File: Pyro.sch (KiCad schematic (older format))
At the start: 14 parts

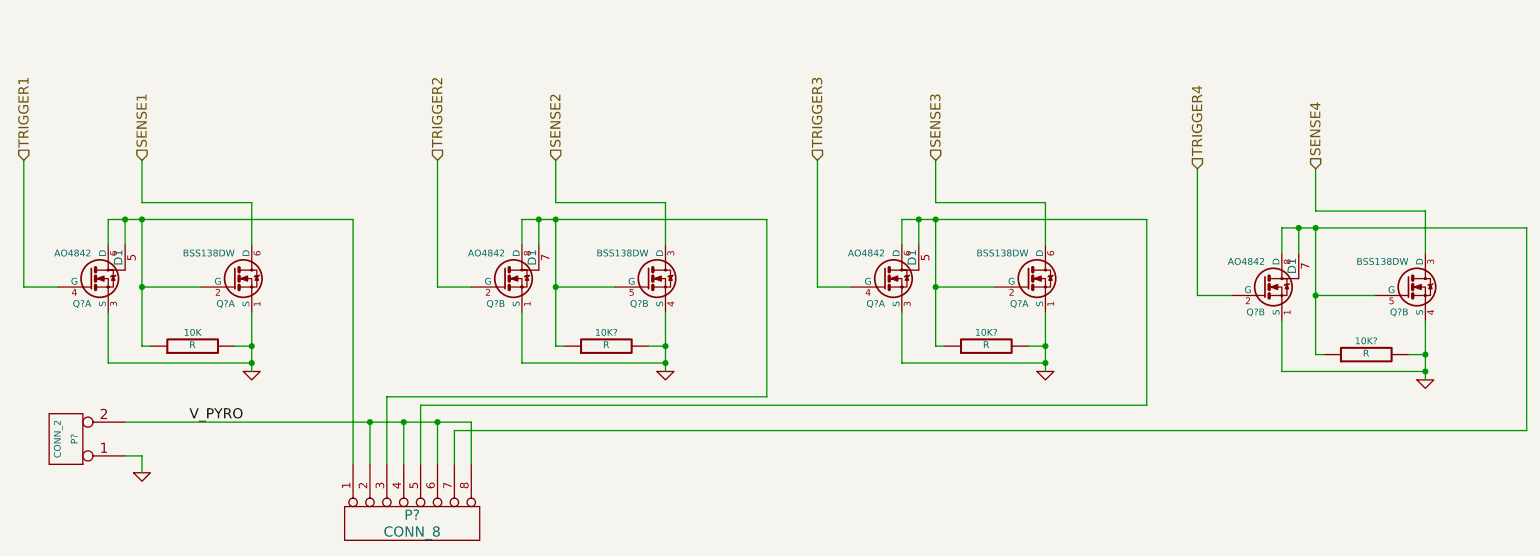
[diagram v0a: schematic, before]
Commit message: Added pyro circuits
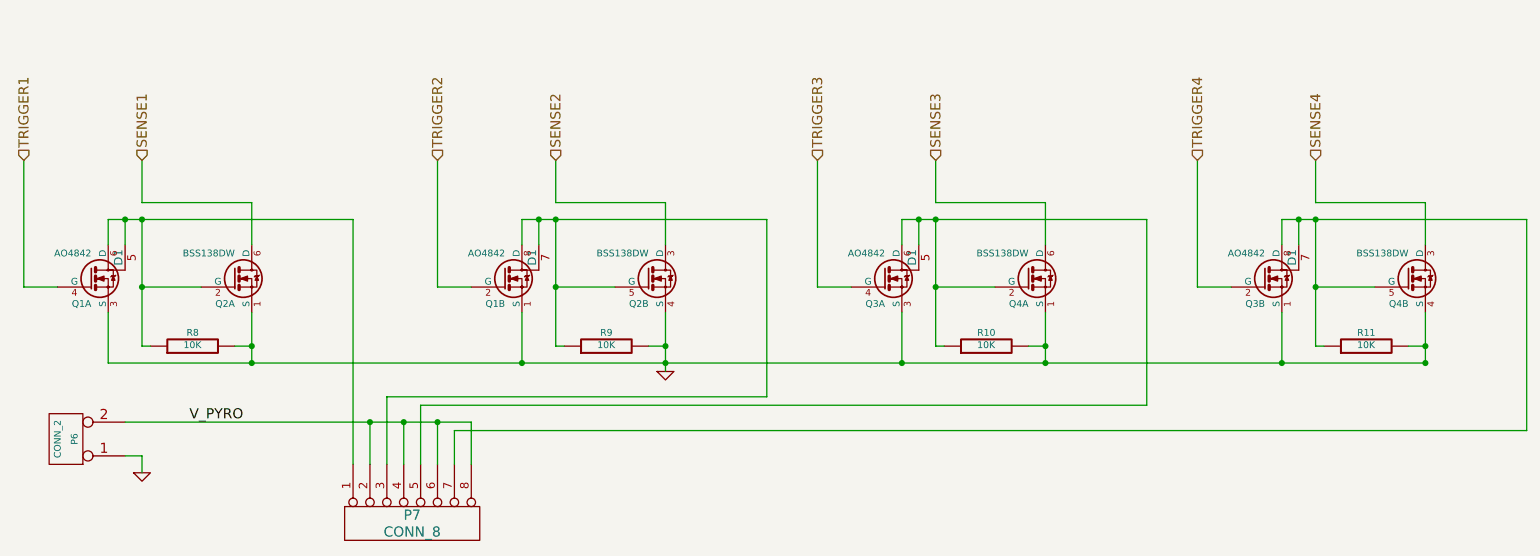
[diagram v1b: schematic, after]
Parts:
- P6: renamed from P?; footprint (none) -> Pin_Headers:Pin_Header_Straight_1x02
- P7: renamed from P?; footprint (none) -> Pin_Headers:Pin_Header_Straight_1x08
- Q1, Q3: renamed from Q?; footprint (none) -> Housings_SOIC:SOIC-8_3.9x4.9mm_Pitch1.27mm
- Q2, Q4: renamed from Q?; footprint (none) -> Housings_SOT-23_SOT-143_TSOT-6:SC70-6_Handsoldering
- R10, R11, R9: renamed from 10K?; value R -> 10K; footprint ~ -> Resistors_SMD:R_0805_HandSoldering
- R8: renamed from 10K; value R -> 10K; footprint ~ -> Resistors_SMD:R_0805_HandSoldering
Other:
- moved on the sheet: Q3B, Q4B, R11

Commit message: New MOSFETs
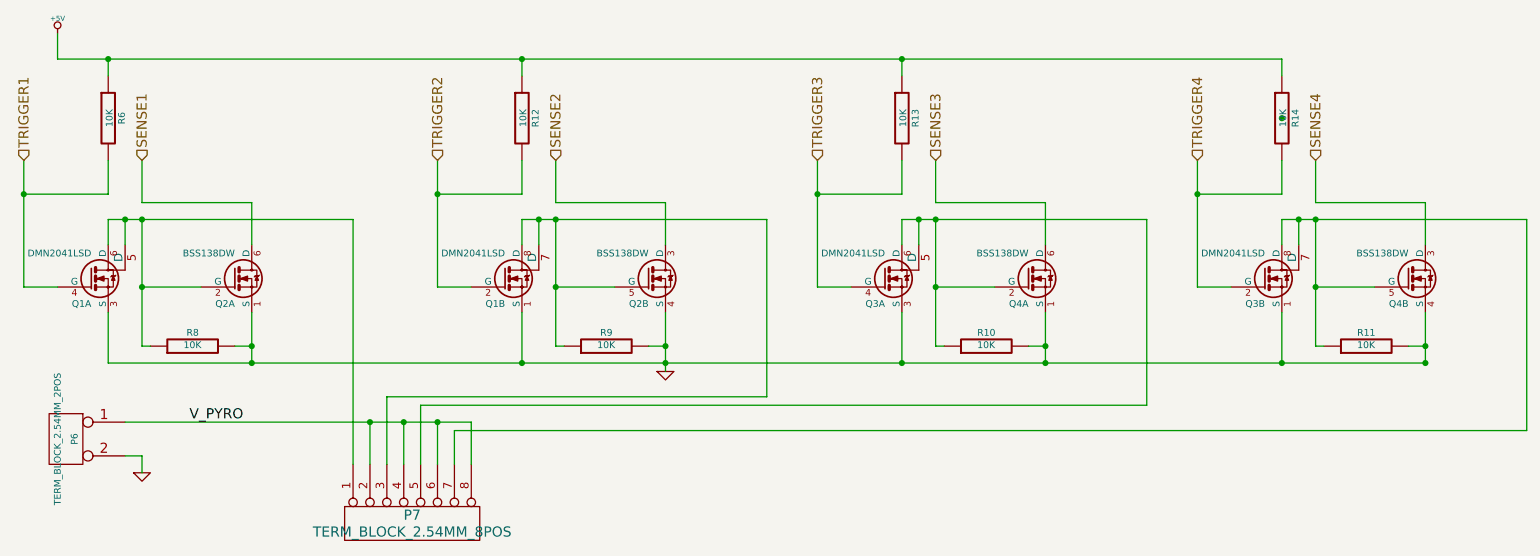
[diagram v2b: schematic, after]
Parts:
- removed P6: CONN_2, Pin_Headers:Pin_Header_Straight_1x02, symbol CONN_2
- removed P7: CONN_8, Pin_Headers:Pin_Header_Straight_1x08, symbol CONN_8
- removed Q1, Q3: AO4842, Housings_SOIC:SOIC-8_3.9x4.9mm_Pitch1.27mm, symbol AO4842
- added P6: TERM_BLOCK_2.54MM_2POS, symbol TERM_BLOCK_2.54MM_2POS
- added P7: TERM_BLOCK_2.54MM_8POS, symbol TERM_BLOCK_2.54MM_8POS
- added Q1, Q3: DMN2041LSD, symbol DMN2041LSD
- added R12, R13, R14, R6: 10K, ~, symbol R
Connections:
- net GND: now also P6.2 (PM), Q1.1 (S), Q1.3 (S), Q3.1 (S), Q3.3 (S)
- net TRIGGER1: now also Q1.4 (G), R6.2
- net TRIGGER2: now also Q1.2 (G), R12.2
- net TRIGGER3: now also Q3.4 (G), R13.2
- net TRIGGER4: now also Q3.2 (G), R14.2
- net V_PYRO: now also P6.1 (P1), P7.2 (P2), P7.4 (P4), P7.6 (P6), P7.8 (P8)
- net at Q2.2 (G), R8.1: now also P7.1 (P1), Q1.5 (D), Q1.6 (D)
- net at Q2.5 (G), R9.1: now also P7.3 (P3), Q1.7 (D), Q1.8 (D)
- net at Q4.2 (G), R10.1: now also P7.5 (P5), Q3.5 (D), Q3.6 (D)
- net at Q4.5 (G), R11.1: now also P7.7 (P7), Q3.7 (D), Q3.8 (D)
- new net +5V: R12.1, R13.1, R14.1, R6.1
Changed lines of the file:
@@
 LIBS:xbee
 LIBS:avbay-cache
-EELAYER 25 0
+EELAYER 27 0
 EELAYER END
 $Descr A4 11693 8268
@@
 Sheet 4 4
 Title ""
-Date "4 dec 2014"
+Date "6 dec 2014"
 Rev ""
 Comp ""
@@
 TRIGGER1
 $Comp
-L CONN_2 P6
-U 1 1 548101EA
-P 950 3400
-F 0 "P6" V 900 3400 40  0000 C CNN
-F 1 "CONN_2" V 1000 3400 40  0000 C CNN
-F 2 "Pin_Headers:Pin_Header_Straight_1x02" H 950 3400 60  0001 C CNN
-F 3 "" H 950 3400 60  0000 C CNN
-	1    950  3400
-	-1   0    0    1
-$EndComp
-$Comp
-L GND #PWR030
+L GND #PWR31
 U 1 1 54810205
 P 1400 3600
-F 0 "#PWR030" H 1400 3600 30  0001 C CNN
+F 0 "#PWR31" H 1400 3600 30  0001 C CNN
 F 1 "GND" H 1400 3530 30  0001 C CNN
 F 2 "" H 1400 3600 60  0000 C CNN
@@
 	1    1400 3600
 	1    0    0    -1
-$EndComp
-$Comp
-L CONN_8 P7
-U 1 1 54810218
-P 3000 3900
-F 0 "P7" V 2950 3900 60  0000 C CNN
-F 1 "CONN_8" V 3050 3900 60  0000 C CNN
-F 2 "Pin_Headers:Pin_Header_Straight_1x08" H 3000 3900 60  0001 C CNN
-F 3 "" H 3000 3900 60  0000 C CNN
-	1    3000 3900
-	0    -1   1    0
 $EndComp
 $Comp
@@
 $EndComp
 $Comp
-L AO4842 Q1
-U 1 1 54810736
-P 1100 2450
-F 0 "Q1" H 1100 2301 40  0000 R CNN
-F 1 "AO4842" H 1100 2600 40  0000 R CNN
-F 2 "Housings_SOIC:SOIC-8_3.9x4.9mm_Pitch1.27mm" H 970 2552 29  0001 C CNN
-F 3 "~" H 1100 2450 60  0000 C CNN
-	1    1100 2450
-	1    0    0    -1
-$EndComp
-$Comp
 L BSS138DW Q2
 U 1 1 54810890
@@
 TRIGGER2
 $Comp
-L GND #PWR031
+L GND #PWR32
 U 1 1 54810E85
 P 4500 3000
-F 0 "#PWR031" H 4500 3000 30  0001 C CNN
+F 0 "#PWR32" H 4500 3000 30  0001 C CNN
 F 1 "GND" H 4500 2930 30  0001 C CNN
 F 2 "" H 4500 3000 60  0000 C CNN
@@
 $EndComp
 $Comp
-L AO4842 Q3
-U 1 1 54810F68
-P 5800 2450
-F 0 "Q3" H 5800 2301 40  0000 R CNN
-F 1 "AO4842" H 5800 2600 40  0000 R CNN
-F 2 "Housings_SOIC:SOIC-8_3.9x4.9mm_Pitch1.27mm" H 5670 2552 29  0001 C CNN
-F 3 "~" H 5800 2450 60  0000 C CNN
-	1    5800 2450
-	1    0    0    -1
-$EndComp
-$Comp
 L BSS138DW Q4
 U 1 1 54810F77
@@
 $EndComp
 $Comp
-L AO4842 Q3
-U 2 1 54810FE4
-P 8050 2450
-F 0 "Q3" H 8050 2301 40  0000 R CNN
-F 1 "AO4842" H 8050 2600 40  0000 R CNN
-F 2 "Housings_SOIC:SOIC-8_3.9x4.9mm_Pitch1.27mm" H 7920 2552 29  0001 C CNN
-F 3 "~" H 8050 2450 60  0000 C CNN
-	2    8050 2450
-	1    0    0    -1
-$EndComp
-$Comp
 L BSS138DW Q4
 U 2 1 54810FF3
@@
 	1    0    0    -1
 $EndComp
-$Comp
-L AO4842 Q1
-U 2 1 548110D2
-P 3550 2450
-F 0 "Q1" H 3550 2301 40  0000 R CNN
-F 1 "AO4842" H 3550 2600 40  0000 R CNN
-F 2 "Housings_SOIC:SOIC-8_3.9x4.9mm_Pitch1.27mm" H 3420 2552 29  0001 C CNN
-F 3 "~" H 3550 2450 60  0000 C CNN
-	2    3550 2450
-	1    0    0    -1
-$EndComp
 Text Label 2000 3300 2    60   ~ 0
 V_PYRO
@@
 Wire Wire Line
 	9000 2950 9000 2650
+Wire Wire Line
+	900  1000 900  1150
+Wire Wire Line
+	900  1150 8150 1150
+$Comp
+L R R6
+U 1 1 548277E3
+P 1200 1500
+F 0 "R6" V 1280 1500 40  0000 C CNN
+F 1 "10K" V 1207 1501 40  0000 C CNN
+F 2 "~" V 1130 1500 30  0000 C CNN
+F 3 "~" H 1200 1500 30  0000 C CNN
+	1    1200 1500
+	1    0    0    -1
+$EndComp
+Wire Wire Line
+	1200 1750 1200 1950
+Wire Wire Line
+	1200 1950 700  1950
+Connection ~ 700  1950
+Wire Wire Line
+	1200 1250 1200 1150
+Connection ~ 1200 1150
+$Comp
+L R R12
+U 1 1 548278C1
+P 3650 1500
+F 0 "R12" V 3730 1500 40  0000 C CNN
+F 1 "10K" V 3657 1501 40  0000 C CNN
+F 2 "~" V 3580 1500 30  0000 C CNN
+F 3 "~" H 3650 1500 30  0000 C CNN
+	1    3650 1500
+	1    0    0    -1
+$EndComp
+$Comp
+L R R14
+U 1 1 548278CC
+P 8150 1500
+F 0 "R14" V 8230 1500 40  0000 C CNN
+F 1 "10K" V 8157 1501 40  0000 C CNN
+F 2 "~" V 8080 1500 30  0000 C CNN
+F 3 "~" H 8150 1500 30  0000 C CNN
+	1    8150 1500
+	1    0    0    -1
+$EndComp
+$Comp
+L R R13
+U 1 1 548278D2
+P 5900 1500
+F 0 "R13" V 5980 1500 40  0000 C CNN
+F 1 "10K" V 5907 1501 40  0000 C CNN
+F 2 "~" V 5830 1500 30  0000 C CNN
+F 3 "~" H 5900 1500 30  0000 C CNN
+	1    5900 1500
+	1    0    0    -1
+$EndComp
+Wire Wire Line
+	8150 1150 8150 1250
+Wire Wire Line
+	8150 1750 8150 1950
+Wire Wire Line
+	8150 1950 7650 1950
+Connection ~ 7650 1950
+Wire Wire Line
+	5900 1150 5900 1250
+Connection ~ 5900 1150
+Wire Wire Line
+	5900 1750 5900 1950
+Wire Wire Line
+	5900 1950 5400 1950
+Connection ~ 5400 1950
+Wire Wire Line
+	3650 1750 3650 1950
+Wire Wire Line
+	3650 1950 3150 1950
+Connection ~ 3150 1950
+Wire Wire Line
+	3650 1250 3650 1150
+Connection ~ 3650 1150
+$Comp
+L +5V #PWR30
+U 1 1 5482887D
+P 900 1000
+F 0 "#PWR30" H 900 1090 20  0001 C CNN
+F 1 "+5V" H 900 1090 30  0000 C CNN
+F 2 "" H 900 1000 60  0000 C CNN
+F 3 "" H 900 1000 60  0000 C CNN
+	1    900  1000
+	1    0    0    -1
+$EndComp
+$Comp
+L TERM_BLOCK_2.54MM_2POS P6
+U 1 1 5482AD9E
+P 950 3400
+F 0 "P6" V 900 3400 40  0000 C CNN
+F 1 "TERM_BLOCK_2.54MM_2POS" V 1000 3400 40  0000 C CNN
+F 2 "" H 950 3400 60  0000 C CNN
+F 3 "" H 950 3400 60  0000 C CNN
+	1    950  3400
+	-1   0    0    -1
+$EndComp
+$Comp
+L TERM_BLOCK_2.54MM_8POS P7
+U 1 1 5482ADAD
+P 3000 3900
+F 0 "P7" V 2950 3900 60  0000 C CNN
+F 1 "TERM_BLOCK_2.54MM_8POS" V 3050 3900 60  0000 C CNN
+F 2 "" H 3000 3900 60  0000 C CNN
+F 3 "" H 3000 3900 60  0000 C CNN
+	1    3000 3900
+	0    -1   1    0
+$EndComp
+Connection ~ 8150 1500
+$Comp
+L DMN2041LSD Q1
+U 1 1 5482D60C
+P 1100 2450
+F 0 "Q1" H 1100 2301 40  0000 R CNN
+F 1 "DMN2041LSD" H 1100 2600 40  0000 R CNN
+F 2 "" H 970 2552 29  0000 C CNN
+F 3 "" H 1100 2450 60  0000 C CNN
+	1    1100 2450
+	1    0    0    -1
+$EndComp
+$Comp
+L DMN2041LSD Q3
+U 1 1 5482D619
+P 5800 2450
+F 0 "Q3" H 5800 2301 40  0000 R CNN
+F 1 "DMN2041LSD" H 5800 2600 40  0000 R CNN
+F 2 "" H 5670 2552 29  0000 C CNN
+F 3 "" H 5800 2450 60  0000 C CNN
+	1    5800 2450
+	1    0    0    -1
+$EndComp
+$Comp
+L DMN2041LSD Q1
+U 2 1 5482D61F
+P 3550 2450
+F 0 "Q1" H 3550 2301 40  0000 R CNN
+F 1 "DMN2041LSD" H 3550 2600 40  0000 R CNN
+F 2 "" H 3420 2552 29  0000 C CNN
+F 3 "" H 3550 2450 60  0000 C CNN
+	2    3550 2450
+	1    0    0    -1
+$EndComp
+$Comp
+L DMN2041LSD Q3
+U 2 1 5482D62A
+P 8050 2450
+F 0 "Q3" H 8050 2301 40  0000 R CNN
+F 1 "DMN2041LSD" H 8050 2600 40  0000 R CNN
+F 2 "" H 7920 2552 29  0000 C CNN
+F 3 "" H 8050 2450 60  0000 C CNN
+	2    8050 2450
+	1    0    0    -1
+$EndComp
 $EndSCHEMATC

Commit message: Improved schematic
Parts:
- removed R12, R13, R14, R6: 10K, ~, symbol R
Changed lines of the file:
@@
 Connection ~ 4500 2850
-Wire Wire Line
-	3150 1750 3150 2500
 Wire Wire Line
 	3150 2500 3350 2500
@@
 Wire Wire Line
 	9000 2950 9000 2650
-Wire Wire Line
-	900  1000 900  1150
-Wire Wire Line
-	900  1150 8150 1150
-$Comp
-L R R6
-U 1 1 548277E3
-P 1200 1500
-F 0 "R6" V 1280 1500 40  0000 C CNN
-F 1 "10K" V 1207 1501 40  0000 C CNN
-F 2 "~" V 1130 1500 30  0000 C CNN
-F 3 "~" H 1200 1500 30  0000 C CNN
-	1    1200 1500
-	1    0    0    -1
-$EndComp
-Wire Wire Line
-	1200 1750 1200 1950
-Wire Wire Line
-	1200 1950 700  1950
-Connection ~ 700  1950
-Wire Wire Line
-	1200 1250 1200 1150
-Connection ~ 1200 1150
-$Comp
-L R R12
-U 1 1 548278C1
-P 3650 1500
-F 0 "R12" V 3730 1500 40  0000 C CNN
-F 1 "10K" V 3657 1501 40  0000 C CNN
-F 2 "~" V 3580 1500 30  0000 C CNN
-F 3 "~" H 3650 1500 30  0000 C CNN
-	1    3650 1500
-	1    0    0    -1
-$EndComp
-$Comp
-L R R14
-U 1 1 548278CC
-P 8150 1500
-F 0 "R14" V 8230 1500 40  0000 C CNN
-F 1 "10K" V 8157 1501 40  0000 C CNN
-F 2 "~" V 8080 1500 30  0000 C CNN
-F 3 "~" H 8150 1500 30  0000 C CNN
-	1    8150 1500
-	1    0    0    -1
-$EndComp
-$Comp
-L R R13
-U 1 1 548278D2
-P 5900 1500
-F 0 "R13" V 5980 1500 40  0000 C CNN
-F 1 "10K" V 5907 1501 40  0000 C CNN
-F 2 "~" V 5830 1500 30  0000 C CNN
-F 3 "~" H 5900 1500 30  0000 C CNN
-	1    5900 1500
-	1    0    0    -1
-$EndComp
-Wire Wire Line
-	8150 1150 8150 1250
-Wire Wire Line
-	8150 1750 8150 1950
-Wire Wire Line
-	8150 1950 7650 1950
-Connection ~ 7650 1950
-Wire Wire Line
-	5900 1150 5900 1250
-Connection ~ 5900 1150
-Wire Wire Line
-	5900 1750 5900 1950
-Wire Wire Line
-	5900 1950 5400 1950
-Connection ~ 5400 1950
-Wire Wire Line
-	3650 1750 3650 1950
-Wire Wire Line
-	3650 1950 3150 1950
-Connection ~ 3150 1950
-Wire Wire Line
-	3650 1250 3650 1150
-Connection ~ 3650 1150
-$Comp
-L +5V #PWR30
-U 1 1 5482887D
-P 900 1000
-F 0 "#PWR30" H 900 1090 20  0001 C CNN
-F 1 "+5V" H 900 1090 30  0000 C CNN
-F 2 "" H 900 1000 60  0000 C CNN
-F 3 "" H 900 1000 60  0000 C CNN
-	1    900  1000
-	1    0    0    -1
-$EndComp
 $Comp
 L TERM_BLOCK_2.54MM_2POS P6
@@
 	0    -1   1    0
 $EndComp
-Connection ~ 8150 1500
 $Comp
 L DMN2041LSD Q1
@@
 	1    0    0    -1
 $EndComp
+Wire Wire Line
+	3150 1750 3150 2500
 $EndSCHEMATC
